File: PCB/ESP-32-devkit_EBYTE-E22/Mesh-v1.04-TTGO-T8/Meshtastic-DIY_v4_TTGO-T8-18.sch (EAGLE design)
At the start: 20 parts

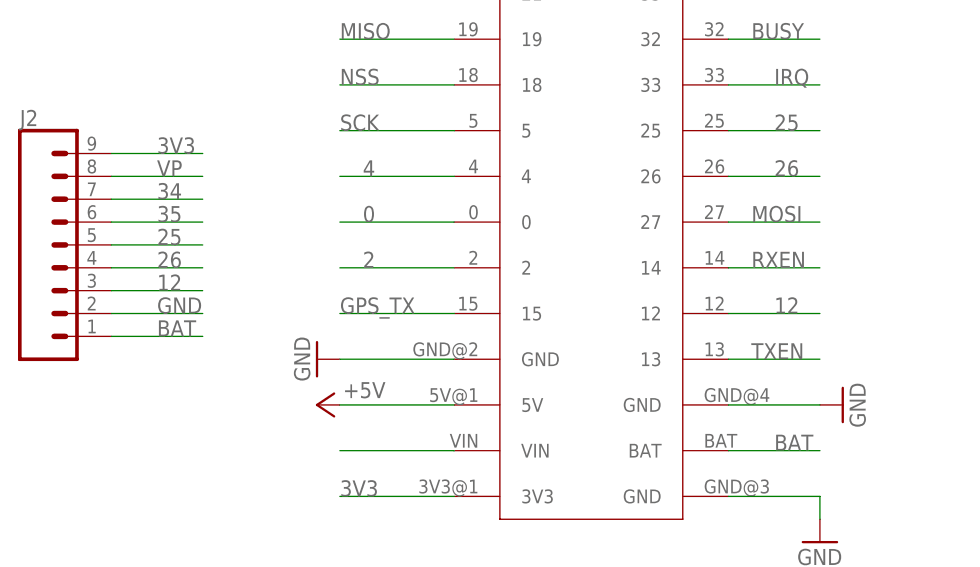
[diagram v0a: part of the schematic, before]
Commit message: [PCB] Fixed `v1.04-TTGO-T8` & description update (#12)
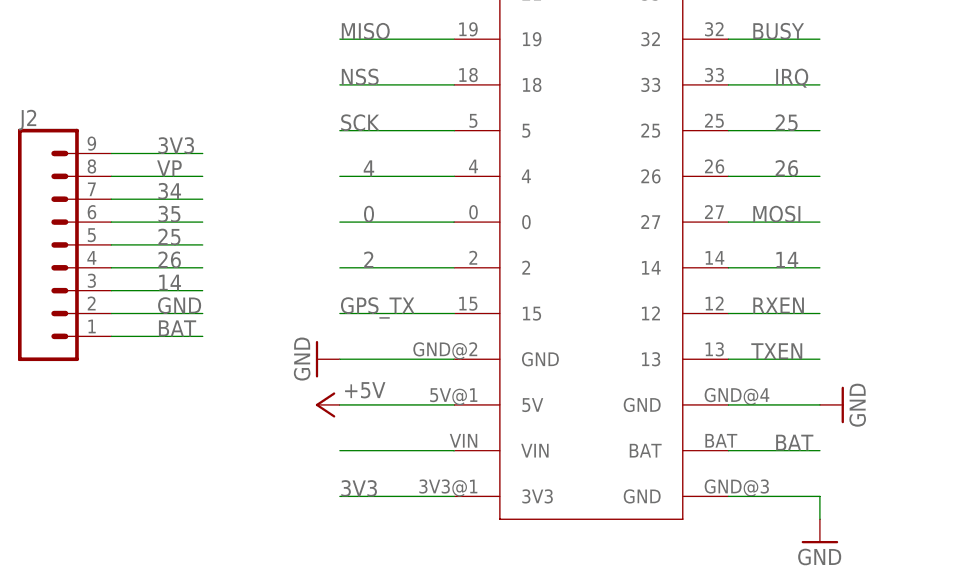
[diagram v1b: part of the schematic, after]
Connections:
- removed net 12: J2.3, TTGO-T8_V1.8.12
- new net 14: J2.3, TTGO-T8_V1.8.14
- net RXEN: now also TTGO-T8_V1.8.12; no longer TTGO-T8_V1.8.14
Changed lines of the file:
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@@
 </segment>
 <segment>
-<pinref part="TTGO-T8_V1.8" gate="G$1" pin="14"/>
-<wire x1="106.68" y1="33.02" x2="116.84" y2="33.02" width="0.1524" layer="91"/>
-<label x="109.22" y="33.02" size="1.778" layer="95"/>
+<pinref part="TTGO-T8_V1.8" gate="G$1" pin="12"/>
+<wire x1="106.68" y1="27.94" x2="116.84" y2="27.94" width="0.1524" layer="91"/>
+<label x="109.22" y="27.94" size="1.778" layer="95"/>
 </segment>
 </net>
@@
 </segment>
 </net>
-<net name="12" class="0">
-<segment>
-<pinref part="TTGO-T8_V1.8" gate="G$1" pin="12"/>
-<wire x1="106.68" y1="27.94" x2="116.84" y2="27.94" width="0.1524" layer="91"/>
-<label x="111.76" y="27.94" size="1.778" layer="95"/>
-</segment>
+<net name="3V3" class="0">
+<segment>
+<pinref part="TTGO-T8_V1.8" gate="G$1" pin="3V3@1"/>
+<wire x1="76.2" y1="7.62" x2="63.5" y2="7.62" width="0.1524" layer="91"/>
+<label x="63.5" y="7.62" size="1.778" layer="95"/>
+</segment>
+<segment>
+<pinref part="J2" gate="G$1" pin="9"/>
+<wire x1="38.1" y1="45.72" x2="48.26" y2="45.72" width="0.1524" layer="91"/>
+<label x="43.18" y="45.72" size="1.778" layer="95"/>
+</segment>
+</net>
+<net name="BAT" class="0">
+<segment>
+<pinref part="J2" gate="G$1" pin="1"/>
+<wire x1="38.1" y1="25.4" x2="48.26" y2="25.4" width="0.1524" layer="91"/>
+<label x="43.18" y="25.4" size="1.778" layer="95"/>
+</segment>
+<segment>
+<pinref part="TTGO-T8_V1.8" gate="G$1" pin="BAT"/>
+<wire x1="106.68" y1="12.7" x2="116.84" y2="12.7" width="0.1524" layer="91"/>
+<label x="111.76" y="12.7" size="1.778" layer="95"/>
+</segment>
+</net>
+<net name="14" class="0">
 <segment>
 <pinref part="J2" gate="G$1" pin="3"/>
@@
 <label x="43.18" y="30.48" size="1.778" layer="95"/>
 </segment>
-</net>
-<net name="3V3" class="0">
-<segment>
-<pinref part="TTGO-T8_V1.8" gate="G$1" pin="3V3@1"/>
-<wire x1="76.2" y1="7.62" x2="63.5" y2="7.62" width="0.1524" layer="91"/>
-<label x="63.5" y="7.62" size="1.778" layer="95"/>
-</segment>
-<segment>
-<pinref part="J2" gate="G$1" pin="9"/>
-<wire x1="38.1" y1="45.72" x2="48.26" y2="45.72" width="0.1524" layer="91"/>
-<label x="43.18" y="45.72" size="1.778" layer="95"/>
-</segment>
-</net>
-<net name="BAT" class="0">
-<segment>
-<pinref part="J2" gate="G$1" pin="1"/>
-<wire x1="38.1" y1="25.4" x2="48.26" y2="25.4" width="0.1524" layer="91"/>
-<label x="43.18" y="25.4" size="1.778" layer="95"/>
-</segment>
-<segment>
-<pinref part="TTGO-T8_V1.8" gate="G$1" pin="BAT"/>
-<wire x1="106.68" y1="12.7" x2="116.84" y2="12.7" width="0.1524" layer="91"/>
-<label x="111.76" y="12.7" size="1.778" layer="95"/>
-</segment>
-</net>
+<segment>
+<pinref part="TTGO-T8_V1.8" gate="G$1" pin="14"/>
+<wire x1="106.68" y1="33.02" x2="116.84" y2="33.02" width="0.1524" layer="91"/>
+<label x="111.76" y="33.02" size="1.778" layer="95"/>
+</segment>
+</net>
